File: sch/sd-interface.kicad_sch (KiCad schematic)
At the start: 30 parts

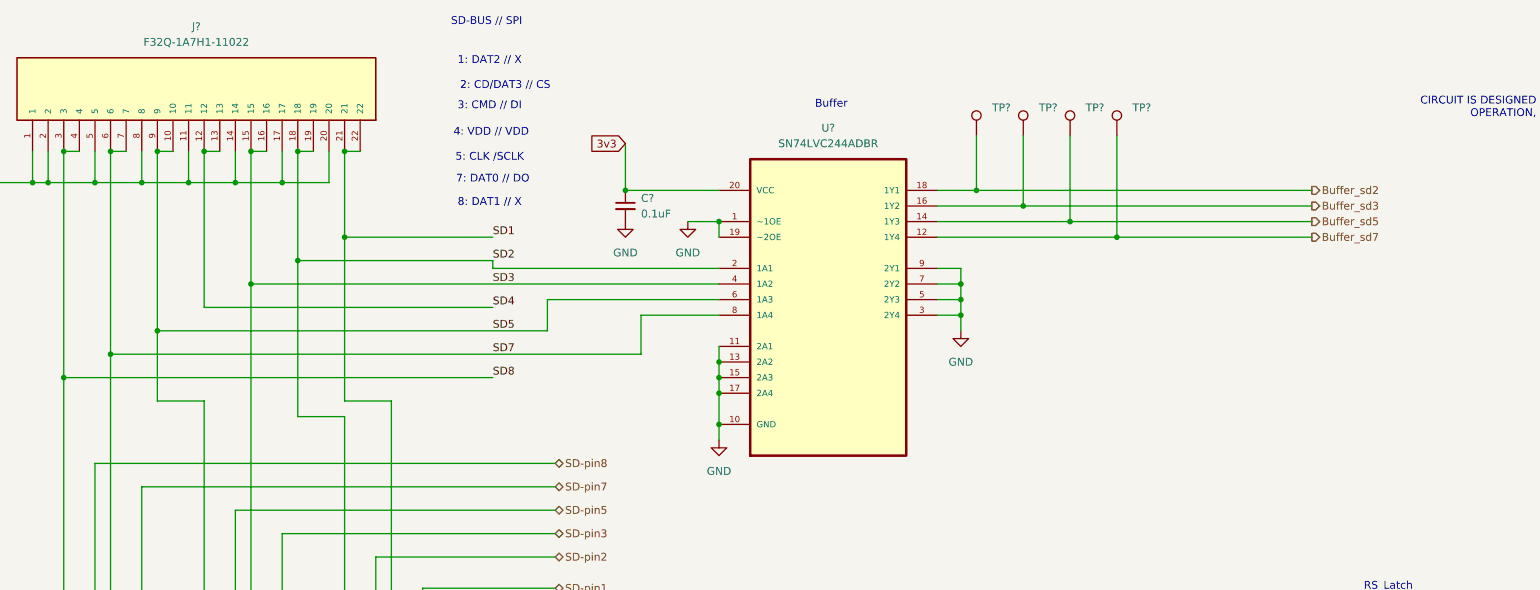
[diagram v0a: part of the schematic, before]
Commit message: changed buffer to level shifter
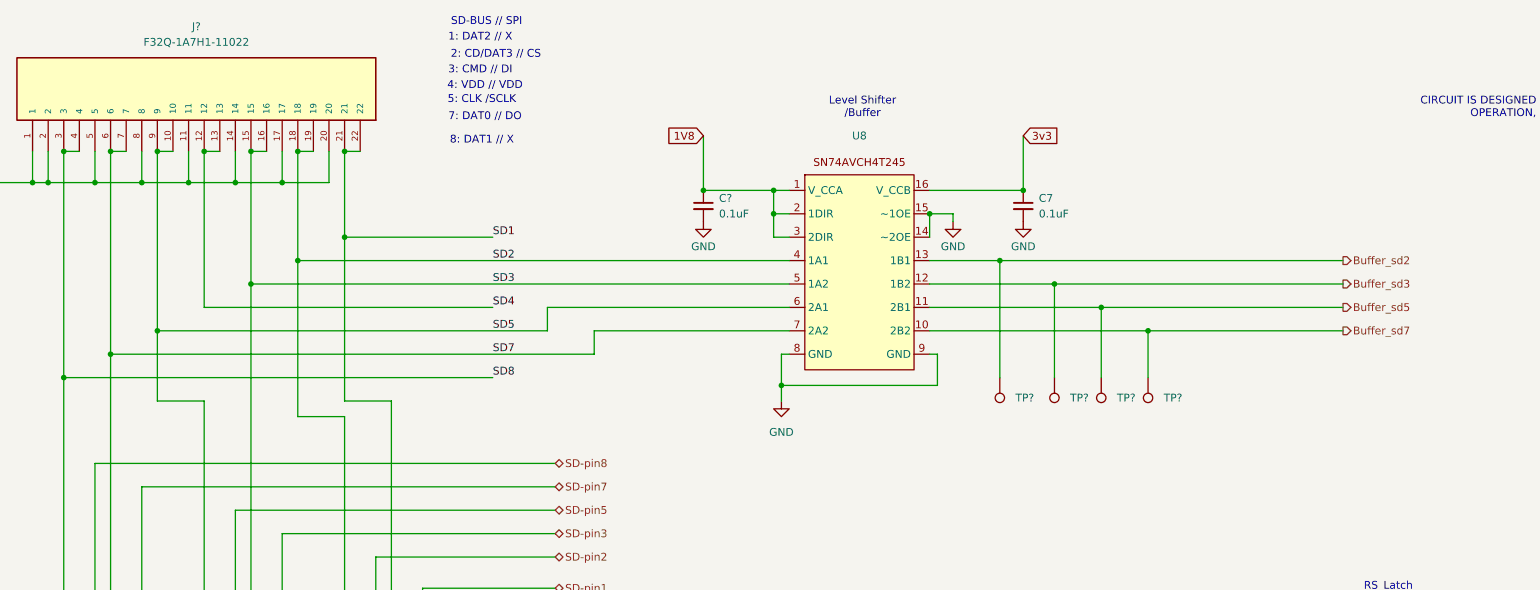
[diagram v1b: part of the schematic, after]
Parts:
- removed U?: SN74LVC244ADBR, SN74LVC244ADBR:SOP65P780X200-20N, symbol SN74LVC244ADBR:SN74LVC244ADBR
- added C7: 0.1uF, Capacitor_SMD:C_0805_2012Metric, symbol Device:C_Small
- added U8: ~, SN74AVCH4T245PW:SOP65P640X120-16N, symbol SN74AVCH4T245PWR:SN74AVCH4T245_
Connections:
- net 3v3: now also C7.1, U8.16 (V_CCB); no longer C?.1
- net Buffer_sd2: now also U8.13 (1B1)
- net Buffer_sd3: now also U8.12 (1B2)
- net Buffer_sd5: now also U8.11 (2B1)
- net Buffer_sd7: now also U8.10 (2B2)
- net GND: now also C7.2, U8.14 (~2OE), U8.15 (~1OE), U8.8 (GND), U8.9 (GND)
- net SD2: now also U8.4 (1A1)
- net SD3: now also U8.5 (1A2)
- net SD5: now also U8.6 (2A1)
- net SD7: now also U8.7 (2A2)
- new net 1V8: C?.1, U8.1 (V_CCA), U8.2 (1DIR), U8.3 (2DIR)
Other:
- note added: "Level Shifter /Buffer"
- note removed: "Buffer"
- moved on the sheet: C?, TP?

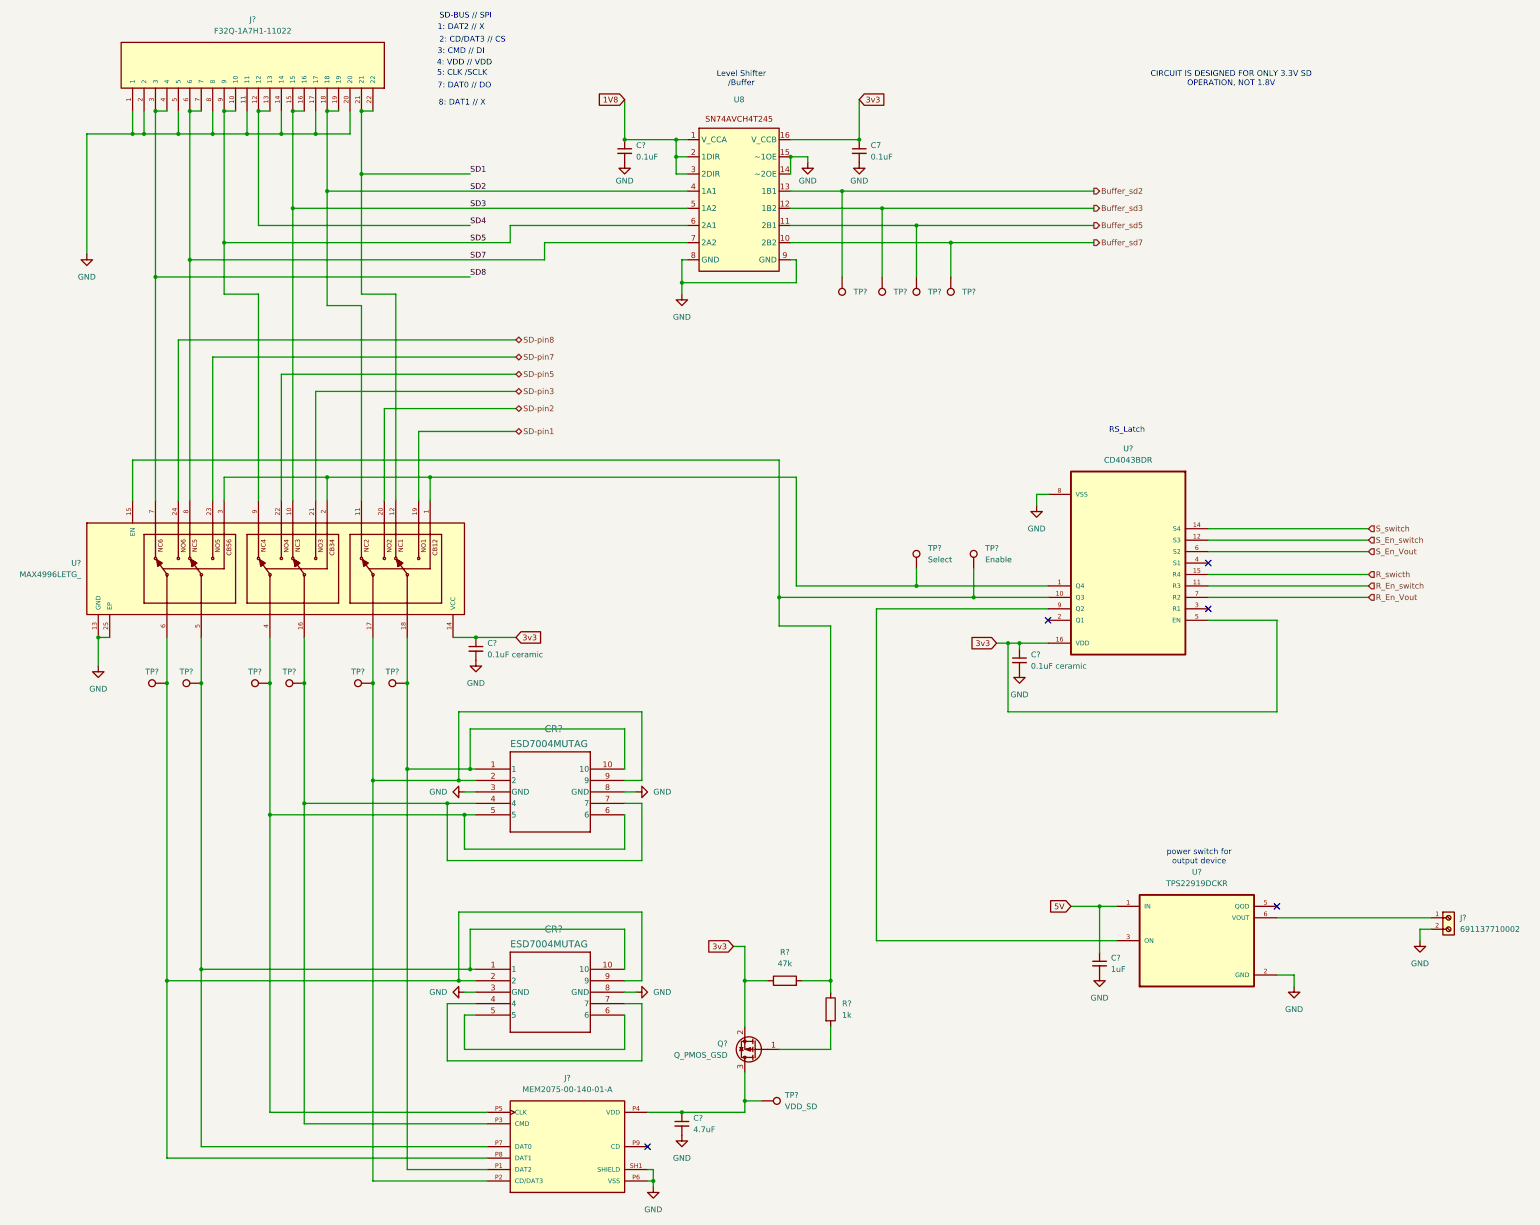
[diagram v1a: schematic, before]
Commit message: added cap footprints and part numbers
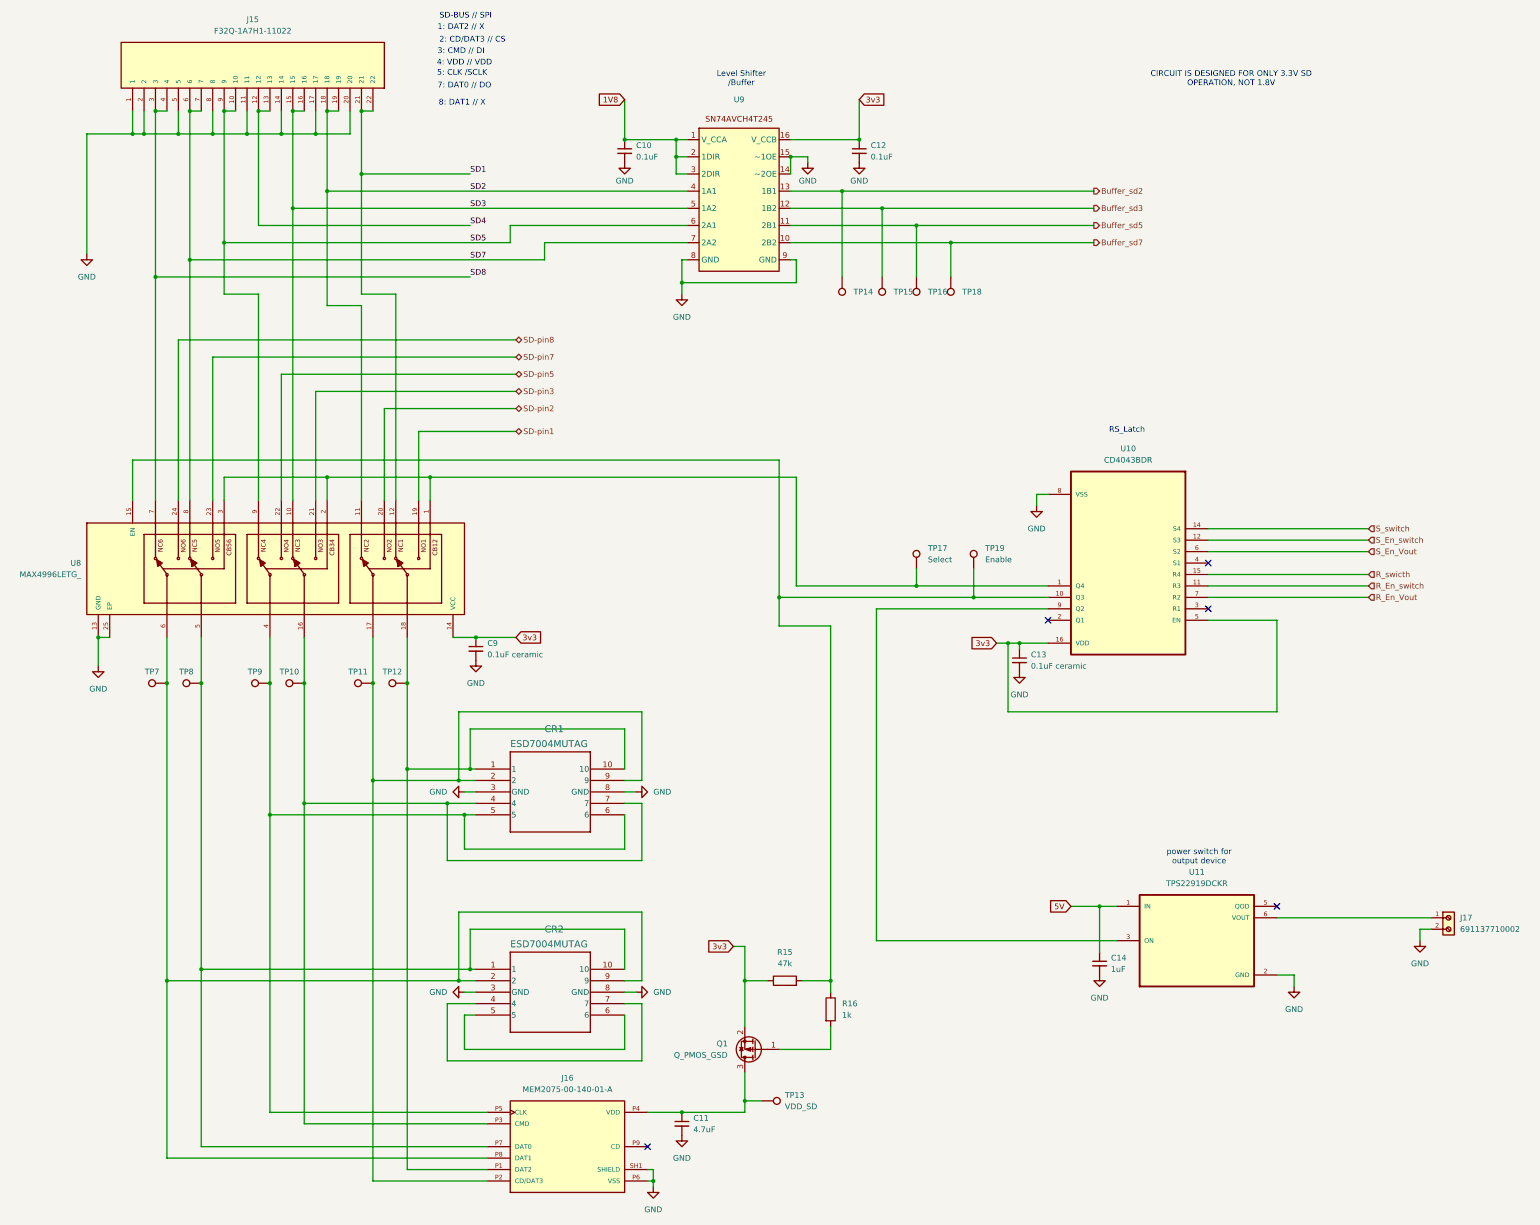
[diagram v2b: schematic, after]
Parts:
- C10, C13, C9: renamed from C?; footprint Capacitor_SMD:C_0805_2012Metric -> Capacitor_SMD:C_0603_1608Metric; MPN (none) -> C0603C104K3RACTU
- C11: renamed from C?; footprint Capacitor_SMD:C_0805_2012Metric -> Capacitor_SMD:C_0603_1608Metric; MPN (none) -> CL10A475KP8NNNC
- C12: renamed from C7; footprint Capacitor_SMD:C_0805_2012Metric -> Capacitor_SMD:C_0603_1608Metric; MPN (none) -> C0603C104K3RACTU
- C14: renamed from C?; footprint Capacitor_SMD:C_0805_2012Metric -> Capacitor_SMD:C_0603_1608Metric; MPN (none) -> CL10B105KP8NNNC
- gave numbers to parts that had none: 24
- renumbered U8 to U9

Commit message: added footprints fore resistors
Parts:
- R15: footprint (none) -> Resistor_SMD:R_0603_1608Metric; MPN (none) -> RC0603FR-0747KL
- R16: footprint (none) -> Resistor_SMD:R_0603_1608Metric; MPN (none) -> RC0603FR-071KL
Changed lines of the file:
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@@
 			)
 		)
-		(property "Footprint" ""
+		(property "Footprint" "Resistor_SMD:R_0603_1608Metric"
 			(at 214.122 236.22 90)
 			(effects
@@
 			)
 		)
+		(property "MPN" "RC0603FR-071KL"
+			(at 215.9 236.22 0)
+			(effects
+				(font
+					(size 1.27 1.27)
+				)
+				(hide yes)
+			)
+		)
 		(pin "1"
 		)
@@
 			)
 		)
-		(property "Footprint" ""
+		(property "Footprint" "Resistor_SMD:R_0603_1608Metric"
 			(at 205.74 231.648 90)
 			(effects
@@
 			(effects
 				(font
+					(size 1.27 1.27)
+				)
+				(hide yes)
+			)
+		)
+		(property "MPN" "RC0603FR-0747KL"
+			(at 205.74 229.87 90)
+			(effects
+				(font

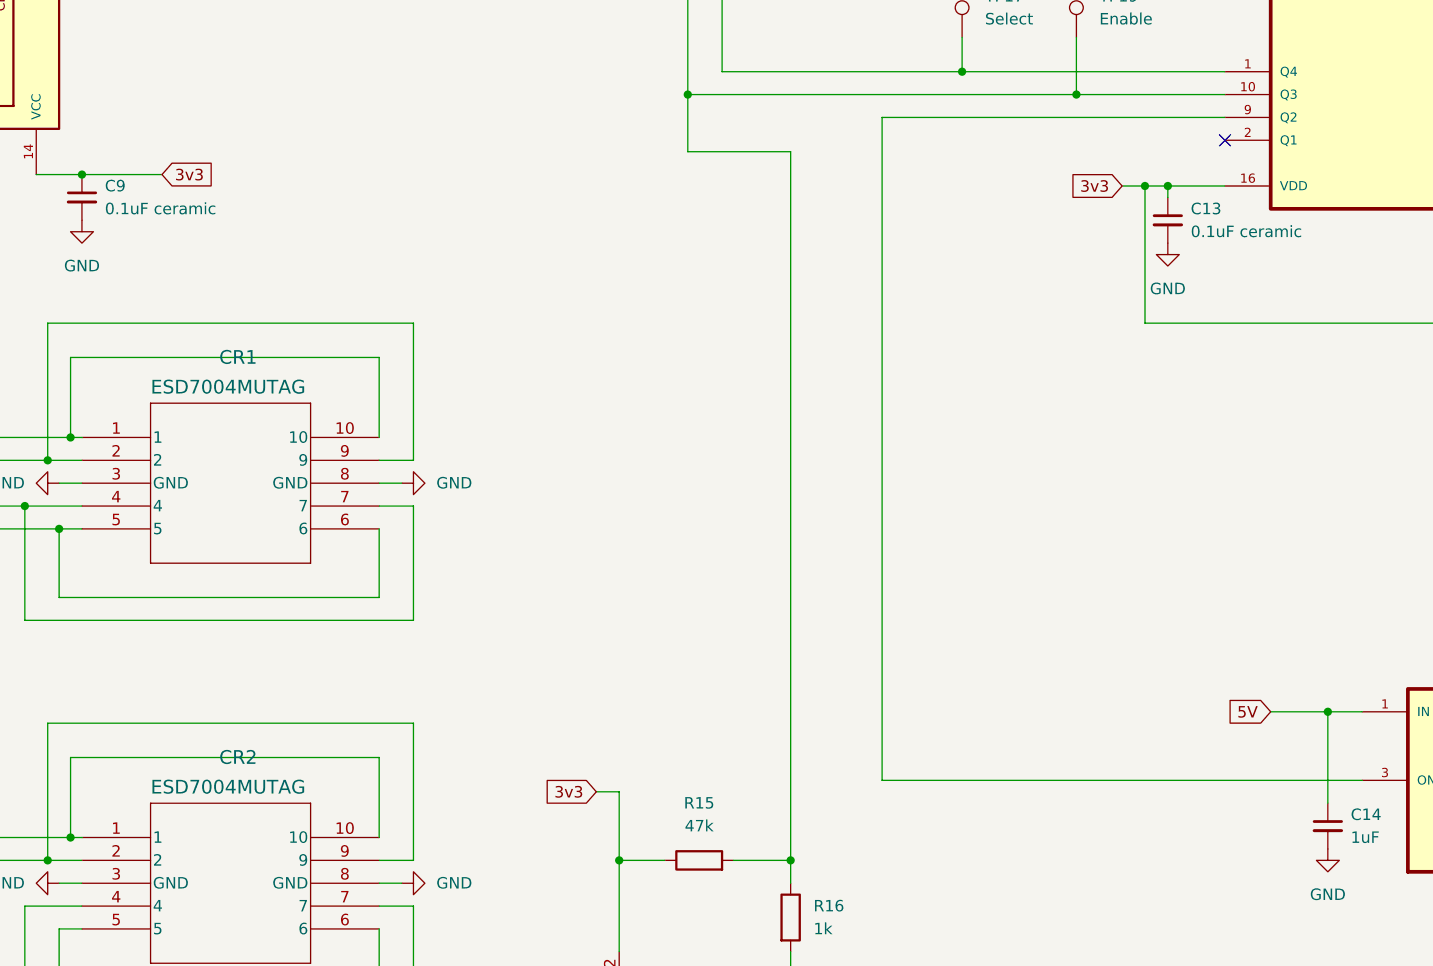
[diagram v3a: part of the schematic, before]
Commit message: added more footprinst and esd
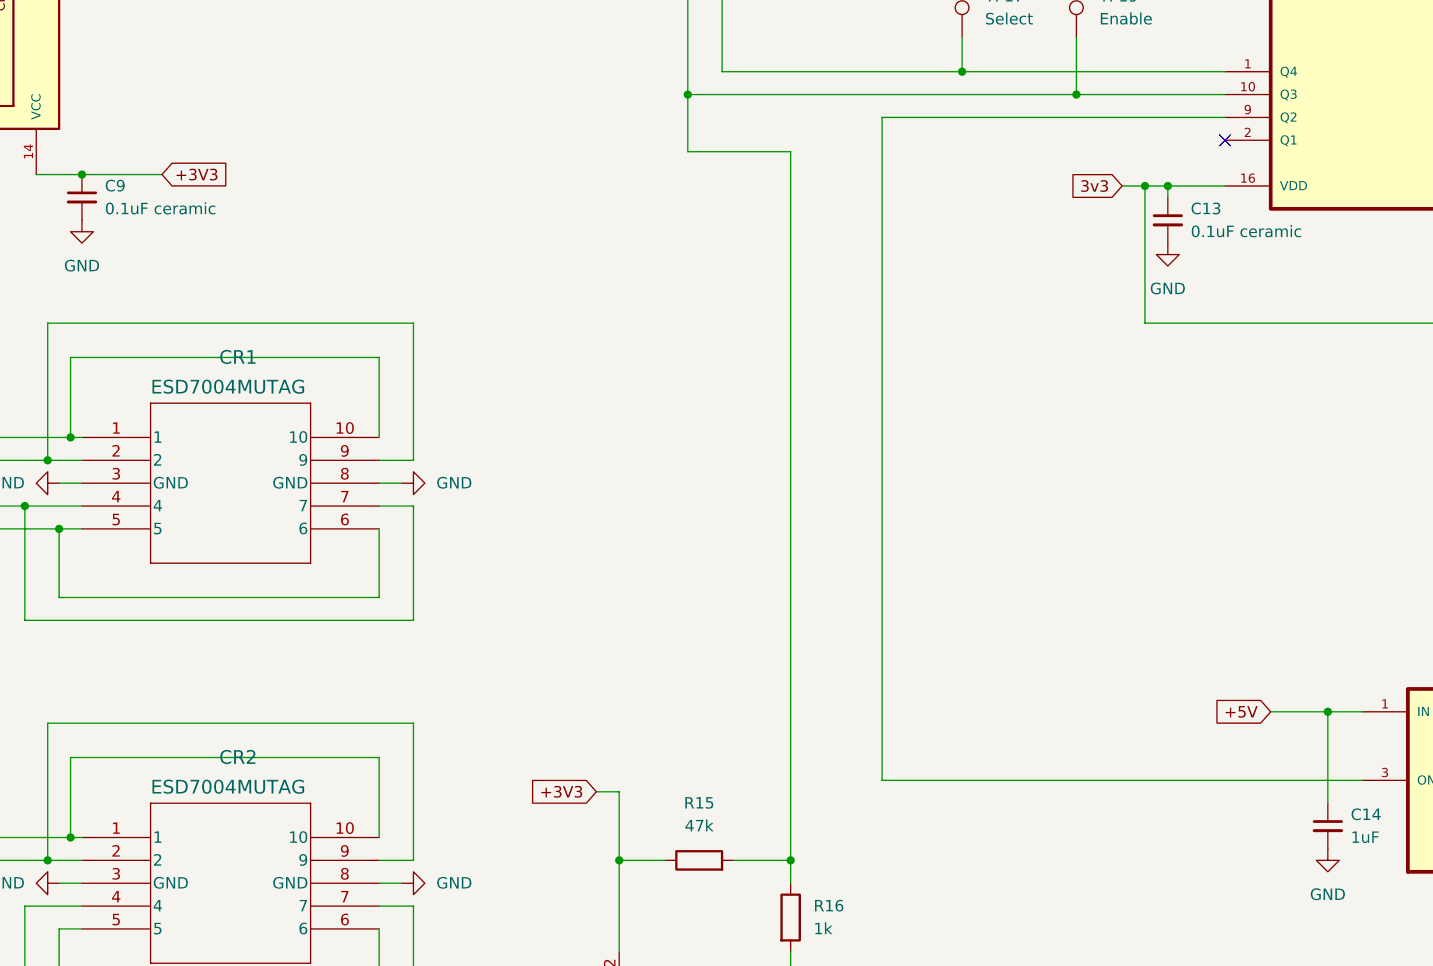
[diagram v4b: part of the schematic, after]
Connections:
- net 3v3: no longer C9.1, Q1.2 (S), R15.1, U8.14 (VCC)
- net 5V renamed +5V
- new net +3V3: C9.1, Q1.2 (S), R15.1, U8.14 (VCC)
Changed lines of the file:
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@@
 		)
 	)
-	(global_label "3v3"
+	(global_label "+3V3"
 		(shape input)
 		(at 146.05 153.67 0)
@@
 		)
 		(property "Intersheetrefs" "${INTERSHEET_REFS}"
-			(at 152.4218 153.67 0)
+			(at 154.1152 153.67 0)
 			(effects
 				(font
@@
 		)
 	)
-	(global_label "5V"
+	(global_label "+5V"
 		(shape input)
 		(at 269.24 213.36 180)
@@
 		)
 		(property "Intersheetrefs" "${INTERSHEET_REFS}"
-			(at 263.9567 213.36 0)
+			(at 262.3843 213.36 0)
 			(effects
 				(font
@@
 		)
 	)
-	(global_label "3v3"
+	(global_label "+3V3"
 		(shape input)
 		(at 194.31 222.25 180)
@@
 		)
 		(property "Intersheetrefs" "${INTERSHEET_REFS}"
-			(at 187.9382 222.25 0)
+			(at 186.2448 222.25 0)
 			(effects
 				(font
